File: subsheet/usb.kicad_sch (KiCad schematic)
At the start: 6 parts, among them J801 USB_C_Receptacle, J802 USB_C_Receptacle, U601 D1213A-04TS-7, U801 D1213A-04TS-7

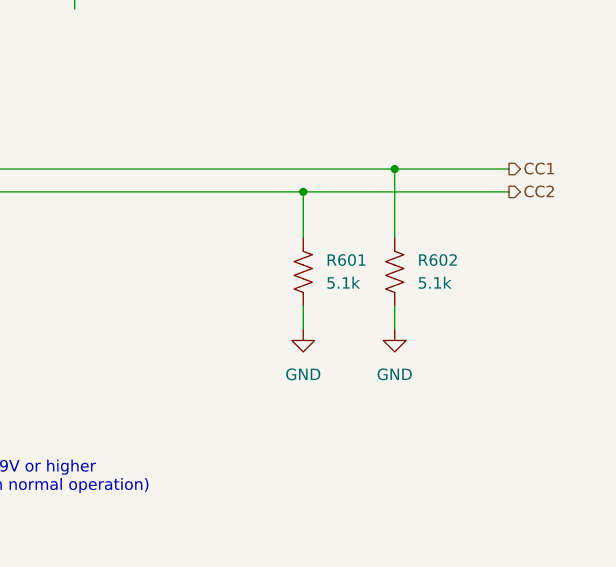
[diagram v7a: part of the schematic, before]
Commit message: Add order codes for all components
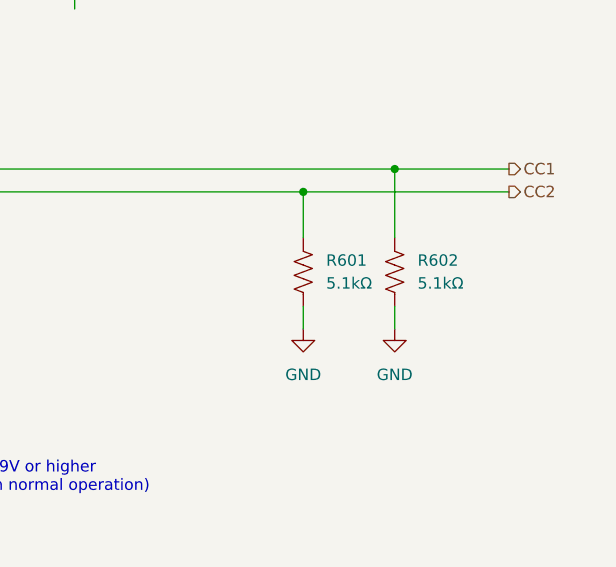
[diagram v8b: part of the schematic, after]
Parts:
- R601, R602: value 5.1k -> 5.1kΩ
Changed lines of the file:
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@@
+			)
+		)
+		(property "I2C address" ""
+			(at -5.08 73.66 0)
+			(effects
+				(font
+					(size 1.27 1.27)
+				)
+				(hide yes)
 			)
 		)
@@
 			)
 		)
+		(property "I2C address" ""
+			(at 27.94 63.5 0)
+			(effects
+				(font
+					(size 1.27 1.27)
+				)
+				(hide yes)
+			)
+		)
 		(pin "A1"
 		)
@@
 			)
 		)
-		(property "Value" "5.1k"
+		(property "Value" "5.1kΩ"
 			(at 167.64 68.5799 0)
 			(effects
@@
 		(property "LCSC" "C23186"
 			(at 165.1 67.31 90)
+			(effects
+				(font
+					(size 1.27 1.27)
+				)
+				(hide yes)
+			)
+		)
+		(property "I2C address" ""
+			(at 165.1 67.31 0)
 			(effects
 				(font
@@
 			)
 		)
+		(property "I2C address" ""
+			(at 86.36 73.66 0)
+			(effects
+				(font
+					(size 1.27 1.27)
+				)
+				(hide yes)
+			)
+		)
 		(pin "4"
 		)
@@
 			)
 		)
-		(property "Value" "5.1k"
+		(property "Value" "5.1kΩ"
 			(at 157.48 68.5799 0)
 			(effects
@@
 		(property "LCSC" "C23186"
 			(at 154.94 67.31 90)
+			(effects
+				(font
+					(size 1.27 1.27)
+				)
+				(hide yes)
+			)
+		)
+		(property "I2C address" ""
+			(at 154.94 67.31 0)
 			(effects
 				(font
@@
 			(at -40.64 63.5 0)
 			(effects
+				(font
+					(size 1.27 1.27)
+				)
+				(hide yes)
+			)
+		)
+		(property "I2C address" ""
+			(at -40.64 63.5 0)
+			(effects
